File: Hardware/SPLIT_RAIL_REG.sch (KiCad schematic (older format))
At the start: 21 parts, among them Q1 PMOS, U9 TPS65130

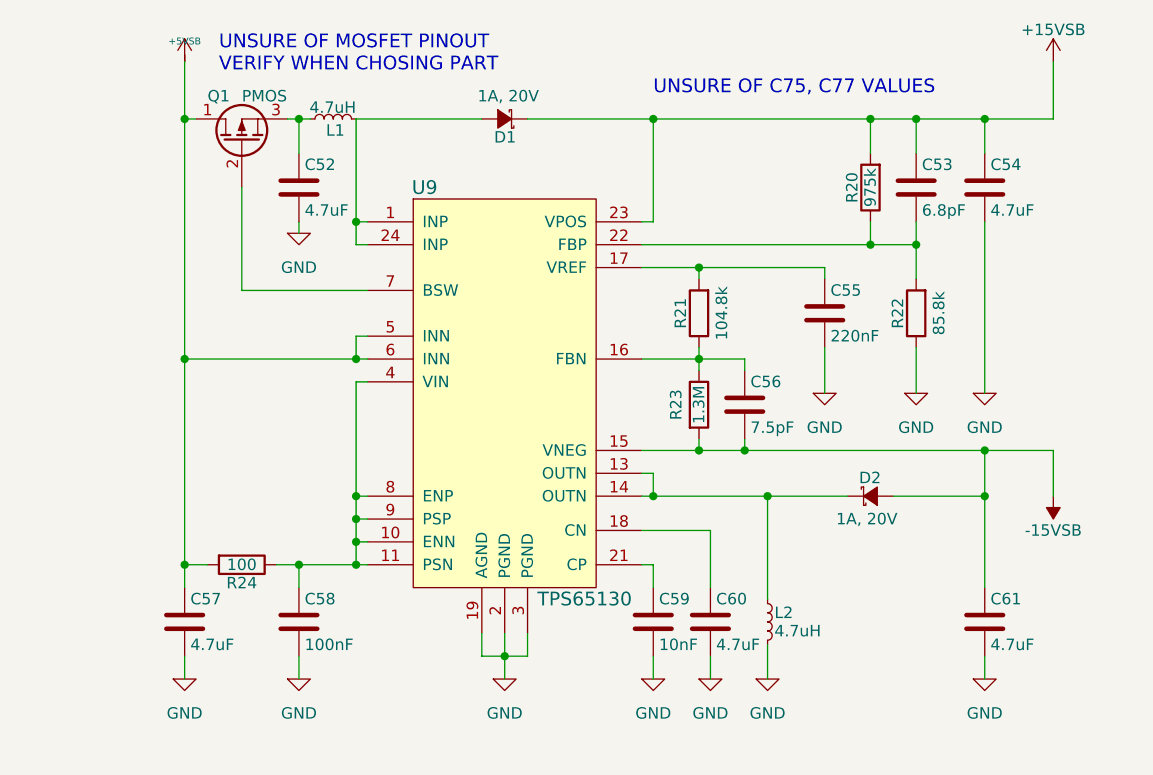
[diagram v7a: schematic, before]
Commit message: Made design review fixes, added breakouts
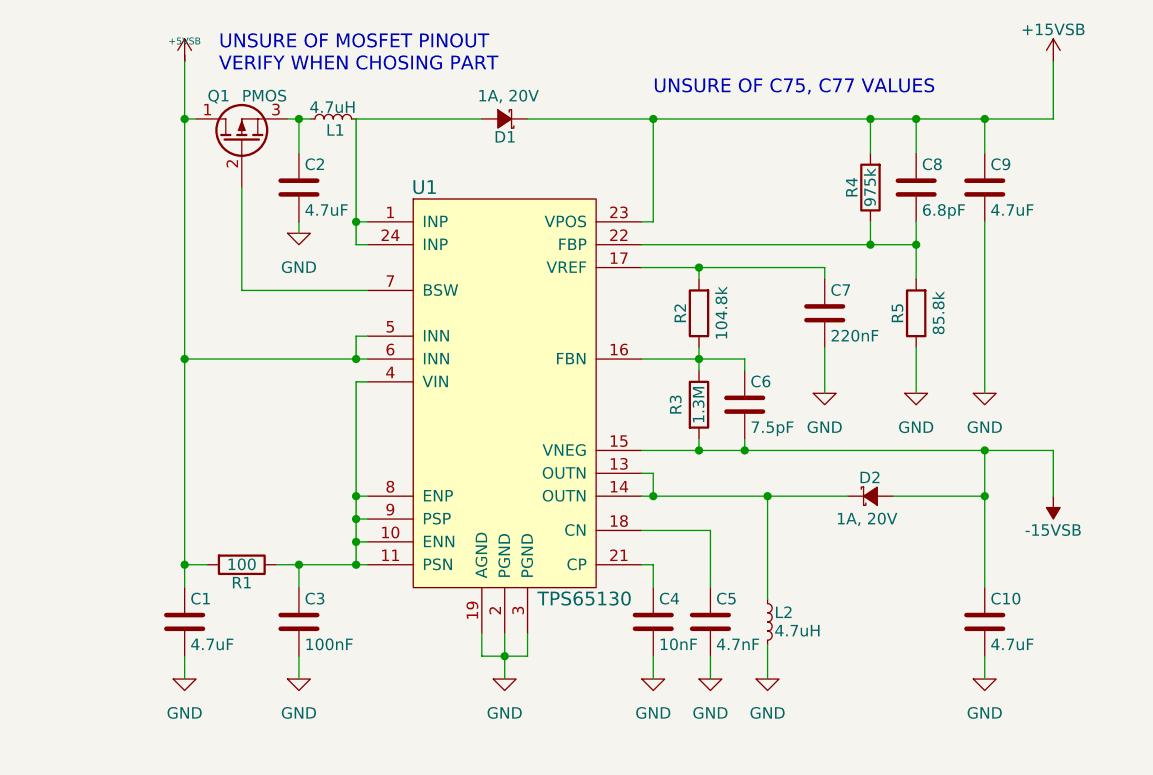
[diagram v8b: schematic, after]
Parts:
- C5: renamed from C60; value 4.7uF -> 4.7nF
- renumbered C57 to C1, C61 to C10, C52 to C2, C58 to C3, C59 to C4, C56 to C6, C55 to C7, C53 to C8, C54 to C9, R24 to R1, R21 to R2, R23 to R3, R20 to R4, R22 to R5, U9 to U1
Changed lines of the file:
@@
 LIBS:microchip_pic18mcu
 LIBS:microchip
-LIBS:microchip1
 LIBS:microcontrollers
 LIBS:motorola
@@
 LIBS:sensors
 LIBS:siliconi
-LIBS:special
 LIBS:stm8
 LIBS:stm32
@@
 $EndDescr
 $Comp
-L TPS65130 U9
+L TPS65130 U1
 U 1 1 57DAC8D6
 P 5050 2900
-F 0 "U9" H 5100 2950 60  0000 C CNN
+F 0 "U1" H 5100 2950 60  0000 C CNN
 F 1 "TPS65130" H 5800 1150 60  0000 C CNN
 F 2 "" H 5050 2900 60  0001 C CNN
@@
 $EndComp
 $Comp
-L GND-RESCUE-museV2 #PWR60
+L GND-RESCUE-museV2 #PWR5
 U 1 1 57DAC9F2
 P 5450 5000
-F 0 "#PWR60" H 5450 4750 50  0001 C CNN
+F 0 "#PWR5" H 5450 4750 50  0001 C CNN
 F 1 "GND" H 5450 4850 50  0000 C CNN
 F 2 "" H 5450 5000 50  0000 C CNN
@@
 $EndComp
 $Comp
-L C-RESCUE-museV2 C59
+L C-RESCUE-museV2 C4
 U 1 1 57DACA1F
 P 6100 4750
-F 0 "C59" H 6125 4850 50  0000 L CNN
+F 0 "C4" H 6125 4850 50  0000 L CNN
 F 1 "10nF" H 6125 4650 50  0000 L CNN
 F 2 "" H 6138 4600 50  0000 C CNN
@@
 $EndComp
 $Comp
-L C-RESCUE-museV2 C60
+L C-RESCUE-museV2 C5
 U 1 1 57DACA4A
 P 6350 4750
-F 0 "C60" H 6375 4850 50  0000 L CNN
-F 1 "4.7uF" H 6375 4650 50  0000 L CNN
+F 0 "C5" H 6375 4850 50  0000 L CNN
+F 1 "4.7nF" H 6375 4650 50  0000 L CNN
 F 2 "" H 6388 4600 50  0000 C CNN
 F 3 "4.7 nF, 50 V, C0G" H 6350 4750 50  0001 C CNN
@@
 $EndComp
 $Comp
-L GND-RESCUE-museV2 #PWR61
+L GND-RESCUE-museV2 #PWR6
 U 1 1 57DACA83
 P 6100 5000
-F 0 "#PWR61" H 6100 4750 50  0001 C CNN
+F 0 "#PWR6" H 6100 4750 50  0001 C CNN
 F 1 "GND" H 6100 4850 50  0000 C CNN
 F 2 "" H 6100 5000 50  0000 C CNN
@@
 $EndComp
 $Comp
-L GND-RESCUE-museV2 #PWR62
+L GND-RESCUE-museV2 #PWR7
 U 1 1 57DACA97
 P 6350 5000
-F 0 "#PWR62" H 6350 4750 50  0001 C CNN
+F 0 "#PWR7" H 6350 4750 50  0001 C CNN
 F 1 "GND" H 6350 4850 50  0000 C CNN
 F 2 "" H 6350 5000 50  0000 C CNN
@@
 $EndComp
 $Comp
-L GND-RESCUE-museV2 #PWR63
+L GND-RESCUE-museV2 #PWR8
 U 1 1 57DACC08
 P 6600 5000
-F 0 "#PWR63" H 6600 4750 50  0001 C CNN
+F 0 "#PWR8" H 6600 4750 50  0001 C CNN
 F 1 "GND" H 6600 4850 50  0000 C CNN
 F 2 "" H 6600 5000 50  0000 C CNN
@@
 $EndComp
 $Comp
-L GND-RESCUE-museV2 #PWR64
+L GND-RESCUE-museV2 #PWR12
 U 1 1 57DACD4E
 P 7550 5000
-F 0 "#PWR64" H 7550 4750 50  0001 C CNN
+F 0 "#PWR12" H 7550 4750 50  0001 C CNN
 F 1 "GND" H 7550 4850 50  0000 C CNN
 F 2 "" H 7550 5000 50  0000 C CNN
@@
 Connection ~ 6100 4200
 $Comp
-L R-RESCUE-museV2 R23
+L R-RESCUE-museV2 R3
 U 1 1 57DACF39
 P 6300 3800
-F 0 "R23" V 6200 3800 50  0000 C CNN
+F 0 "R3" V 6200 3800 50  0000 C CNN
 F 1 "1.3M" V 6300 3800 50  0000 C CNN
 F 2 "" V 6230 3800 50  0000 C CNN
@@
 $EndComp
 $Comp
-L C-RESCUE-museV2 C56
+L C-RESCUE-museV2 C6
 U 1 1 57DACF8B
 P 6500 3800
-F 0 "C56" H 6525 3900 50  0000 L CNN
+F 0 "C6" H 6525 3900 50  0000 L CNN
 F 1 "7.5pF" H 6525 3700 50  0000 L CNN
 F 2 "" H 6538 3650 50  0000 C CNN
@@
 $EndComp
 $Comp
-L R-RESCUE-museV2 R21
+L R-RESCUE-museV2 R2
 U 1 1 57DACFF1
 P 6300 3400
-F 0 "R21" V 6380 3400 50  0000 C CNN
+F 0 "R2" V 6380 3400 50  0000 C CNN
 F 1 "104.8k" V 6200 3400 50  0000 C CNN
 F 2 "" V 6230 3400 50  0000 C CNN
@@
 	6300 3200 6300 3250
 $Comp
-L C-RESCUE-museV2 C55
+L C-RESCUE-museV2 C7
 U 1 1 57DADA01
 P 6850 3400
-F 0 "C55" H 6875 3500 50  0000 L CNN
+F 0 "C7" H 6875 3500 50  0000 L CNN
 F 1 "220nF" H 6875 3300 50  0000 L CNN
 F 2 "" H 6888 3250 50  0000 C CNN
@@
 Connection ~ 6300 3200
 $Comp
-L GND-RESCUE-museV2 #PWR55
+L GND-RESCUE-museV2 #PWR9
 U 1 1 57DADA89
 P 6850 3750
-F 0 "#PWR55" H 6850 3500 50  0001 C CNN
+F 0 "#PWR9" H 6850 3500 50  0001 C CNN
 F 1 "GND" H 6850 3600 50  0000 C CNN
 F 2 "" H 6850 3750 50  0000 C CNN
@@
 Connection ~ 4800 4200
 $Comp
-L C-RESCUE-museV2 C58
+L C-RESCUE-museV2 C3
 U 1 1 57DAE032
 P 4550 4750
-F 0 "C58" H 4575 4850 50  0000 L CNN
+F 0 "C3" H 4575 4850 50  0000 L CNN
 F 1 "100nF" H 4575 4650 50  0000 L CNN
 F 2 "" H 4588 4600 50  0000 C CNN
@@
 Connection ~ 4800 4500
 $Comp
-L R-RESCUE-museV2 R24
+L R-RESCUE-museV2 R1
 U 1 1 57DAE140
 P 4300 4500
-F 0 "R24" V 4380 4500 50  0000 C CNN
+F 0 "R1" V 4380 4500 50  0000 C CNN
 F 1 "100" V 4300 4500 50  0000 C CNN
 F 2 "" V 4230 4500 50  0000 C CNN
@@
 	4050 4500 4150 4500
 $Comp
-L GND-RESCUE-museV2 #PWR59
+L GND-RESCUE-museV2 #PWR4
 U 1 1 57DAE30A
 P 4550 5000
-F 0 "#PWR59" H 4550 4750 50  0001 C CNN
+F 0 "#PWR4" H 4550 4750 50  0001 C CNN
 F 1 "GND" H 4550 4850 50  0000 C CNN
 F 2 "" H 4550 5000 50  0000 C CNN
@@
 	4550 5000 4550 4900
 $Comp
-L GND-RESCUE-museV2 #PWR58
+L GND-RESCUE-museV2 #PWR2
 U 1 1 57DAE3B0
 P 4050 5000
-F 0 "#PWR58" H 4050 4750 50  0001 C CNN
+F 0 "#PWR2" H 4050 4750 50  0001 C CNN
 F 1 "GND" H 4050 4850 50  0000 C CNN
 F 2 "" H 4050 5000 50  0000 C CNN
@@
 Connection ~ 4550 2550
 $Comp
-L C-RESCUE-museV2 C52
+L C-RESCUE-museV2 C2
 U 1 1 57DAEAFC
 P 4550 2850
-F 0 "C52" H 4575 2950 50  0000 L CNN
+F 0 "C2" H 4575 2950 50  0000 L CNN
 F 1 "4.7uF" H 4575 2750 50  0000 L CNN
 F 2 "" H 4588 2700 50  0000 C CNN
@@
 $EndComp
 $Comp
-L GND-RESCUE-museV2 #PWR54
+L GND-RESCUE-museV2 #PWR3
 U 1 1 57DAEBCD
 P 4550 3050
-F 0 "#PWR54" H 4550 2800 50  0001 C CNN
+F 0 "#PWR3" H 4550 2800 50  0001 C CNN
 F 1 "GND" H 4550 2900 50  0000 C CNN
 F 2 "" H 4550 3050 50  0000 C CNN
@@
 Connection ~ 6100 2550
 $Comp
-L R-RESCUE-museV2 R22
+L R-RESCUE-museV2 R5
 U 1 1 57DAF2BE
 P 7250 3400
-F 0 "R22" V 7330 3400 50  0000 C CNN
+F 0 "R5" V 7330 3400 50  0000 C CNN
 F 1 "85.8k" V 7150 3400 50  0000 C CNN
 F 2 "" V 7180 3400 50  0000 C CNN
@@
 $EndComp
 $Comp
-L GND-RESCUE-museV2 #PWR56
+L GND-RESCUE-museV2 #PWR10
 U 1 1 57DAF32E
 P 7250 3750
-F 0 "#PWR56" H 7250 3500 50  0001 C CNN
+F 0 "#PWR10" H 7250 3500 50  0001 C CNN
 F 1 "GND" H 7250 3600 50  0000 C CNN
 F 2 "" H 7250 3750 50  0000 C CNN
@@
 	7250 3000 7250 3250
 $Comp
-L R-RESCUE-museV2 R20
+L R-RESCUE-museV2 R4
 U 1 1 57DAF532
 P 7050 2850
-F 0 "R20" V 7130 2850 50  0000 C CNN
+F 0 "R4" V 7130 2850 50  0000 C CNN
 F 1 "975k" V 7050 2850 50  0000 C CNN
 F 2 "" V 6980 2850 50  0000 C CNN
@@
 Connection ~ 7250 2550
 $Comp
-L C-RESCUE-museV2 C53
+L C-RESCUE-museV2 C8
 U 1 1 57DAF6D3
 P 7250 2850
-F 0 "C53" H 7275 2950 50  0000 L CNN
+F 0 "C8" H 7275 2950 50  0000 L CNN
 F 1 "6.8pF" H 7275 2750 50  0000 L CNN
 F 2 "" H 7288 2700 50  0000 C CNN
@@
 $EndComp
 $Comp
-L C-RESCUE-museV2 C54
+L C-RESCUE-museV2 C9
 U 1 1 57DAF88B
 P 7550 2850
-F 0 "C54" H 7575 2950 50  0000 L CNN
+F 0 "C9" H 7575 2950 50  0000 L CNN
 F 1 "4.7uF" H 7575 2750 50  0000 L CNN
 F 2 "" H 7588 2700 50  0000 C CNN
@@
 Connection ~ 7550 2550
 $Comp
-L GND-RESCUE-museV2 #PWR57
+L GND-RESCUE-museV2 #PWR11
 U 1 1 57DAF96B
 P 7550 3750
-F 0 "#PWR57" H 7550 3500 50  0001 C CNN
+F 0 "#PWR11" H 7550 3500 50  0001 C CNN
 F 1 "GND" H 7550 3600 50  0000 C CNN
 F 2 "" H 7550 3750 50  0000 C CNN
@@
 	7550 3750 7550 3000
 $Comp
-L C-RESCUE-museV2 C57
+L C-RESCUE-museV2 C1
 U 1 1 57DB07FA
 P 4050 4750
-F 0 "C57" H 4075 4850 50  0000 L CNN
+F 0 "C1" H 4075 4850 50  0000 L CNN
 F 1 "4.7uF" H 4075 4650 50  0000 L CNN
 F 2 "" H 4088 4600 50  0000 C CNN
@@
 $EndComp
 $Comp
-L C-RESCUE-museV2 C61
+L C-RESCUE-museV2 C10
 U 1 1 57DB11B4
 P 7550 4750
-F 0 "C61" H 7575 4850 50  0000 L CNN
+F 0 "C10" H 7575 4850 50  0000 L CNN
 F 1 "4.7uF" H 7575 4650 50  0000 L CNN
 F 2 "" H 7588 4600 50  0000 C CNN
@@
 UNSURE OF C75, C77 VALUES
 $Comp
-L +5VSB #PWR?
+L +5VSB #PWR1
 U 1 1 57F87DFC
 P 4050 2300
-F 0 "#PWR?" H 4050 2390 20  0001 C CNN
+F 0 "#PWR1" H 4050 2390 20  0001 C CNN
 F 1 "+5VSB" H 4050 2390 30  0000 C CNN
 F 2 "" H 4050 2300 60  0000 C CNN
@@
 	5550 2550 7850 2550
 $Comp
-L -15VSB #PWR?
+L -15VSB #PWR14
 U 1 1 57F88303
 P 7850 4200
-F 0 "#PWR?" H 7850 4300 50  0001 C CNN
+F 0 "#PWR14" H 7850 4300 50  0001 C CNN
 F 1 "-15VSB" H 7850 4350 50  0000 C CNN
 F 2 "" H 7850 4200 50  0000 C CNN
@@
 	7850 2550 7850 2300
 $Comp
-L +15VSB #PWR?
+L +15VSB #PWR13
 U 1 1 57F88166
 P 7850 2300
-F 0 "#PWR?" H 7850 2150 50  0001 C CNN
+F 0 "#PWR13" H 7850 2150 50  0001 C CNN
 F 1 "+15VSB" H 7850 2440 50  0000 C CNN
 F 2 "" H 7850 2300 50  0000 C CNN
